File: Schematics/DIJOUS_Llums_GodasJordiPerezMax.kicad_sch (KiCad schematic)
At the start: 101 parts, among them J1 Conn_01x05_Socket, J2 Conn_01x03, J3 Conn_01x06, J4 Screw_Terminal_01x02, J5 Conn_01x05, J6 DE9_Plug, J7 Conn_01x02, J8 Conn_01x06_Socket, K1 G5LE-1 DC12, K2 G5LE-1 DC12, Q1 ZXTN19020DFFTA, Q2 ZXTN19020DFFTA, Q3 ZXTN19020DFFTA, Q4 Si7336ADP, Q5 Si7336ADP, Q6 ZXTN19020DFFTA, Q7 ZXTN19020DFFTA, Q8 Si7336ADP, Q9 Si7336ADP, U1 PCA9306D, U2 PIC18F2580-I/SO, U3 LM2596T-ADJ, U5 MCP2551-I-SN, U6 ADM7172ACPZ-5.0-R7, U7 LT6202CS5, U8 TLV1117-33

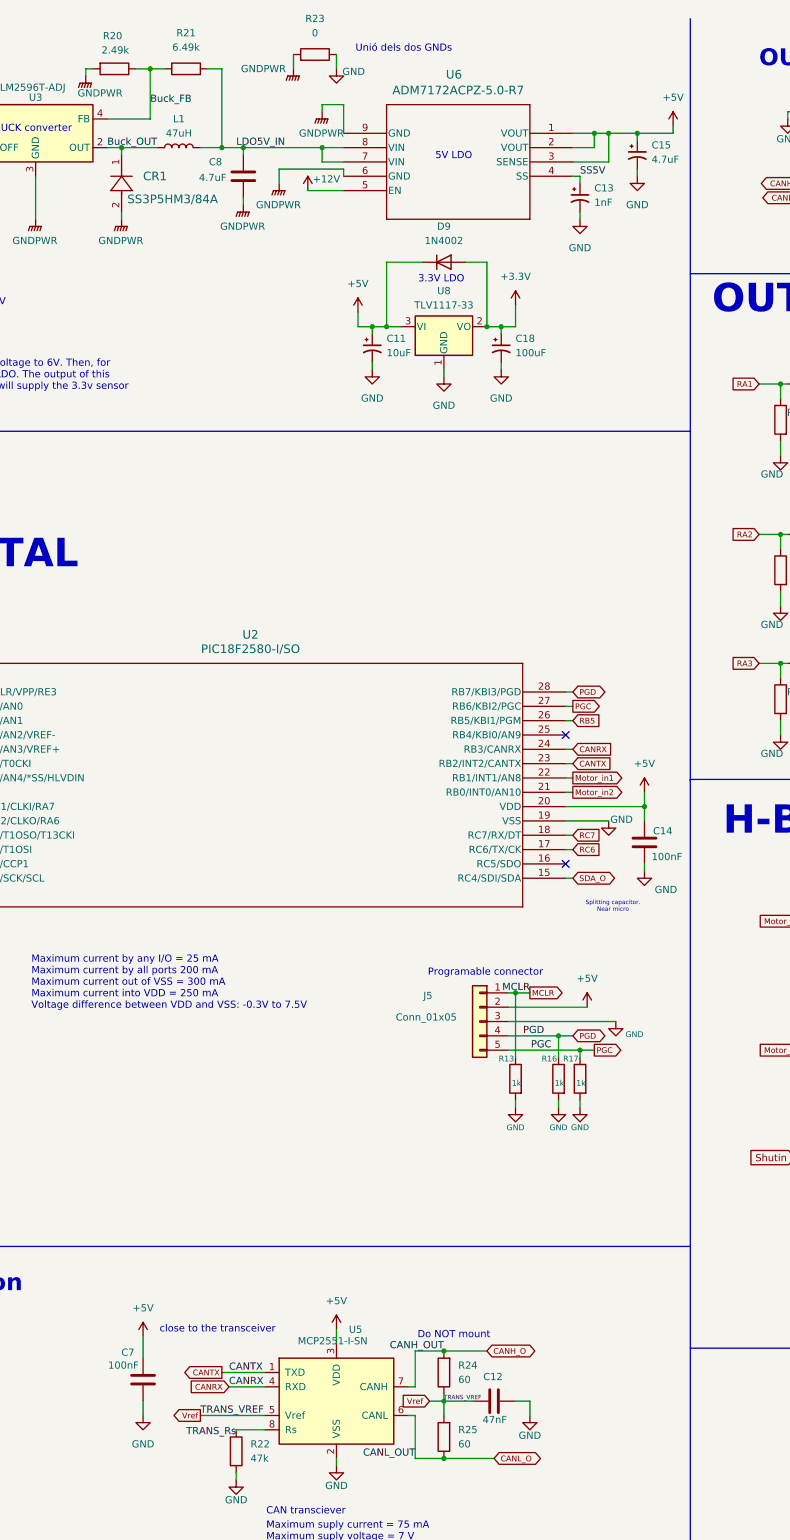
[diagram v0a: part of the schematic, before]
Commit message: Update esquemàtic
S'ha modificat el LDO de 6 a 5V i alguns footprints que no estaven ben assignats
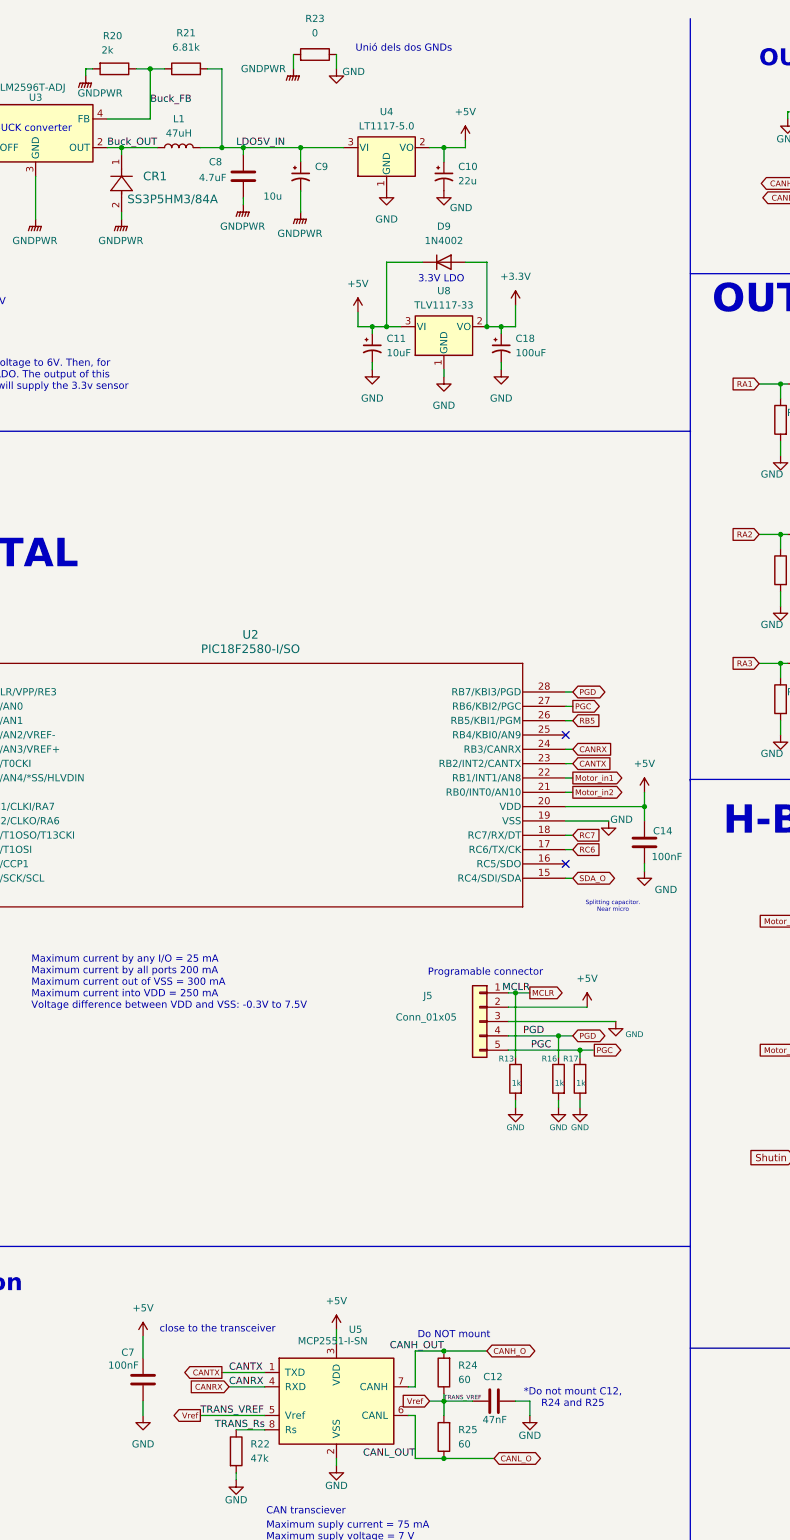
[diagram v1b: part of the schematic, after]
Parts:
- removed C13: 1nF, Capacitor_SMD:C_1206_3216Metric_Pad1.33x1.80mm_HandSolder, symbol Device:C_Polarized_Small_US
- removed C15: 4.7uF, Capacitor_SMD:C_1206_3216Metric_Pad1.33x1.80mm_HandSolder, symbol Device:C_Polarized_Small_US
- removed U6: ADM7172ACPZ-5.0-R7, ADM7172ACPZ-5.0-R7:CP-8-21_ADI, symbol ADM7172ACPZ-5.0-R7:ADM7172ACPZ-5.0-R7
- added C10: 22u, Capacitor_SMD:C_0402_1005Metric, symbol Device:C_Polarized_Small_US
- added C9: 10u, Capacitor_SMD:C_0201_0603Metric, symbol Device:C_Polarized_Small_US
- added U4: LT1117-5.0, Package_TO_SOT_SMD:SOT-223-3_TabPin2, symbol Regulator_Linear:LT1117-5.0
- C11: footprint Capacitor_SMD:C_1206_3216Metric_Pad1.33x1.80mm_HandSolder -> Capacitor_SMD:C_0201_0603Metric
- C18, C6: footprint Capacitor_SMD:C_1206_3216Metric_Pad1.33x1.80mm_HandSolder -> Capacitor_SMD:C_1210_3225Metric
- C8: footprint Capacitor_SMD:C_1206_3216Metric_Pad1.33x1.80mm_HandSolder -> Capacitor_SMD:C_0402_1005Metric
- R11: footprint Resistor_SMD:R_1206_3216Metric -> Capacitor_SMD:C_0805_2012Metric
- R20: value 2.49k -> 2k
- R21: value 6.49k -> 6.81k
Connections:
- net +5V: now also C10.1, U4.2 (VO)
- net GND: now also C10.2, U4.1 (GND)
- net GNDPWR: now also C9.2
- net LDO5V_IN: now also C9.1, U4.3 (VI)
- net TRANS_Rs: now also R22.1, U5.8 (Rs)
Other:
- note added: "*Do not mount C12, R24 and R25"
- note removed: "5V LDO"

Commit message: Add files via upload
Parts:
- C3, C5: footprint Capacitor_SMD:C_1206_3216Metric_Pad1.33x1.80mm_HandSolder -> Capacitor_SMD:C_0603_1608Metric
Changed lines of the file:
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@@
 			)
 		)
-		(property "Footprint" "Capacitor_SMD:C_1206_3216Metric_Pad1.33x1.80mm_HandSolder"
+		(property "Footprint" "Capacitor_SMD:C_0603_1608Metric"
 			(at 127.9652 184.15 0)
 			(effects
@@
 			)
 		)
-		(property "Footprint" "Capacitor_SMD:C_1206_3216Metric_Pad1.33x1.80mm_HandSolder"
+		(property "Footprint" "Capacitor_SMD:C_0603_1608Metric"
 			(at 140.6652 184.15 0)
 			(effects

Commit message: Add files via upload
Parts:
- L1: footprint Inductor_SMD:L_Neosid_Ms42 -> Inductor_SMD:L_1210_3225Metric
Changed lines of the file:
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@@
 			)
 		)
-		(property "Footprint" "Inductor_SMD:L_Neosid_Ms42"
+		(property "Footprint" "Inductor_SMD:L_1210_3225Metric"
 			(at 196.85 35.56 0)
 			(effects
